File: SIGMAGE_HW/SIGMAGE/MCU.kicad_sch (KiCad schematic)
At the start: 28 parts, among them J10 TSW10607GS, J11 HTSW10807GD, J12 HTSW10807GD, J13 HTSW10807GD, J9 TSW10607GS, U8 STM32F407VGTx, X1 STDCSU18M

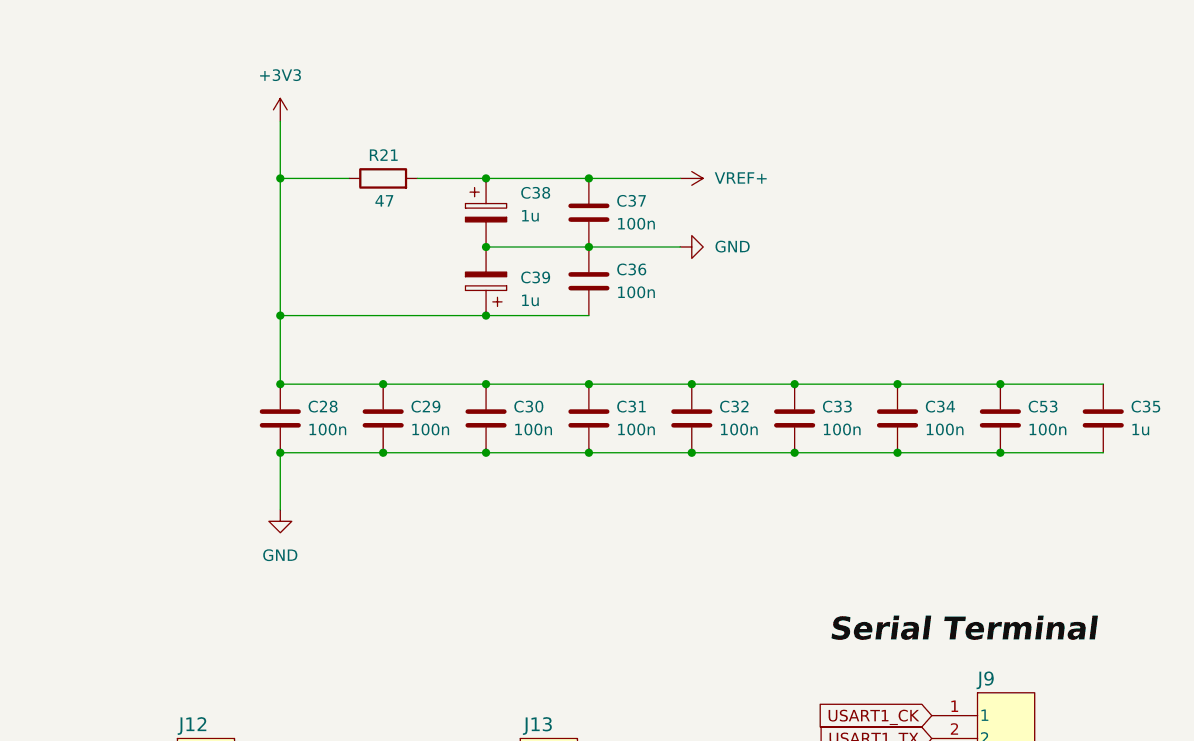
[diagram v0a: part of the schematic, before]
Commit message: More DAC changes
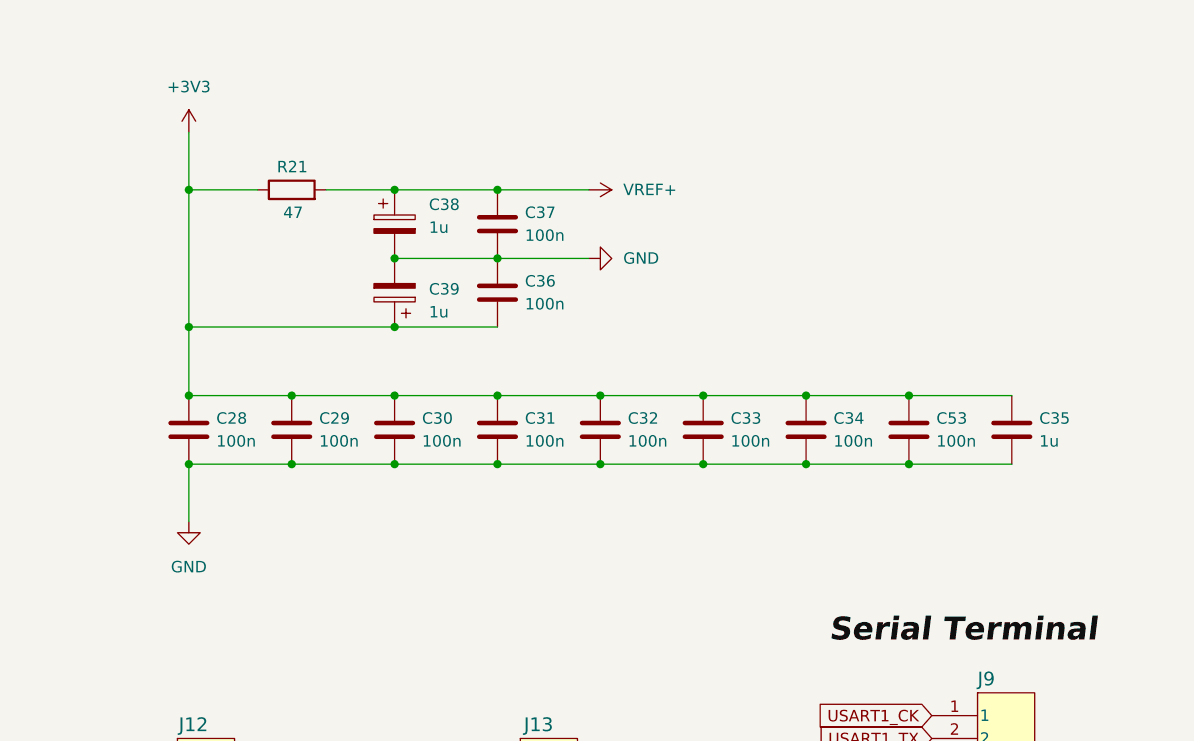
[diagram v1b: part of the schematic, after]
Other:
- moved on the sheet: C28, C29, C30, C31, C32, C33, C34, C35, C36, C37, C38, C39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

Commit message: preps for FPGA
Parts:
- removed J11, J12, J13: HTSW10807GD, SIGMAGE:HTSW10807GD, symbol SIGMAGE:HTSW10807GD
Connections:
- net GPIO_PE0 is gone; now on net ADC1_LRCK: U8.97 (PE0)
- net GPIO_PE1 is gone; now on net ADC2_LRCK: U8.98 (PE1)
- net GPIO_PE2 is gone; now on net ADC1_BYPAS: U8.1 (PE2)
- net GPIO_PE3 is gone; now on net ADC2_BYPAS: U8.2 (PE3)
- net ADC1_BCK: no longer U8.52 (PB13)
- net ADC1_BYPAS: no longer U8.93 (PB7)
- net ADC1_DOUT: no longer U8.54 (PB15)
- net ADC1_LRCK: no longer U8.51 (PB12)
- net ADC1_PDWN: no longer U8.92 (PB6)
- net ADC2_BCK: no longer U8.78 (PC10)
- net ADC2_BYPAS: no longer U8.96 (PB9)
- net ADC2_DOUT: no longer U8.91 (PB5)
- net ADC2_LRCK: no longer U8.29 (PA4)
- net ADC2_PDWN: no longer U8.95 (PB8)
- net ADC2_SCKI: no longer U8.64 (PC7)
- net JTCK_SWCLK: no longer U8.76 (PA14)
- net JTDI: no longer U8.77 (PA15)
- net JTDO_SWO: no longer U8.89 (PB3)
- net JTMS_SWDIO: no longer U8.72 (PA13)
- net JTRST: no longer U8.90 (PB4)
- net PHY_CRS_DV: no longer U8.32 (PA7)
- net PHY_MDC: no longer U8.16 (PC1)
- net PHY_MDIO: no longer U8.25 (PA2)
- net PHY_NRST: no longer U8.47 (PB10)
- net PHY_REFCLK: no longer U8.24 (PA1)
- net PHY_RXD0: no longer U8.33 (PC4)
- net PHY_RXD1: no longer U8.34 (PC5)
- net PHY_TXD0: no longer U8.80 (PC12)
- net PHY_TXD1: no longer U8.7 (PC13)
- net PHY_TXEN: no longer U8.48 (PB11)
- net USART1_CK: no longer U8.67 (PA8)
- net USART1_CTS: no longer U8.70 (PA11)
- net USART1_RTS: no longer U8.71 (PA12)
- net USART1_RX: no longer U8.69 (PA10)
- net USART1_TX: no longer U8.68 (PA9)
- net ADC1_SCKI: no longer names the net of U8.63 (PC6)
- net GPIO_PA0: no longer names the net of U8.23 (PA0)
- net GPIO_PA3: no longer names the net of U8.26 (PA3)
- net GPIO_PA5: no longer names the net of U8.30 (PA5)
- net GPIO_PA6: no longer names the net of U8.31 (PA6)
- net GPIO_PB0: no longer names the net of U8.35 (PB0)
- net GPIO_PB1: no longer names the net of U8.36 (PB1)
- net GPIO_PB14: no longer names the net of U8.53 (PB14)
- net GPIO_PB2: no longer names the net of U8.37 (PB2)
- net GPIO_PC0: no longer names the net of U8.15 (PC0)
- net GPIO_PC11: no longer names the net of U8.79 (PC11)
- net GPIO_PC14: no longer names the net of U8.8 (PC14)
- net GPIO_PC15: no longer names the net of U8.9 (PC15)
- net GPIO_PC2: no longer names the net of U8.17 (PC2)
- net GPIO_PC3: no longer names the net of U8.18 (PC3)
- net GPIO_PC8: no longer names the net of U8.65 (PC8)
- net GPIO_PC9: no longer names the net of U8.66 (PC9)
- net GPIO_PD0: no longer names the net of U8.81 (PD0)
- net GPIO_PD1: no longer names the net of U8.82 (PD1)
- net GPIO_PD10: no longer names the net of U8.57 (PD10)
- net GPIO_PD11: no longer names the net of U8.58 (PD11)
- net GPIO_PD12: no longer names the net of U8.59 (PD12)
- net GPIO_PD13: no longer names the net of U8.60 (PD13)
- net GPIO_PD14: no longer names the net of U8.61 (PD14)
- net GPIO_PD15: no longer names the net of U8.62 (PD15)
- net GPIO_PD2: no longer names the net of U8.83 (PD2)
- net GPIO_PD3: no longer names the net of U8.84 (PD3)
- net GPIO_PD4: no longer names the net of U8.85 (PD4)
- net GPIO_PD5: no longer names the net of U8.86 (PD5)
- net GPIO_PD6: no longer names the net of U8.87 (PD6)
- net GPIO_PD7: no longer names the net of U8.88 (PD7)
- net GPIO_PD8: no longer names the net of U8.55 (PD8)
- net GPIO_PD9: no longer names the net of U8.56 (PD9)
- net GPIO_PE10: no longer names the net of U8.41 (PE10)
- net GPIO_PE11: no longer names the net of U8.42 (PE11)
- net GPIO_PE12: no longer names the net of U8.43 (PE12)
- net GPIO_PE13: no longer names the net of U8.44 (PE13)
- net GPIO_PE14: no longer names the net of U8.45 (PE14)
- net GPIO_PE15: no longer names the net of U8.46 (PE15)
- net GPIO_PE4: no longer names the net of U8.3 (PE4)
- net GPIO_PE5: no longer names the net of U8.4 (PE5)
- net GPIO_PE6: no longer names the net of U8.5 (PE6)
- net GPIO_PE7: no longer names the net of U8.38 (PE7)
- net GPIO_PE8: no longer names the net of U8.39 (PE8)
- net GPIO_PE9: no longer names the net of U8.40 (PE9)

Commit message: some changes
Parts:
- removed C28, C29, C30, C31, C32, C33, C34, C36, C37, C40, C53: 100n, Capacitor_SMD:C_0603_1608Metric, symbol Device:C
- removed C35: 1u, Capacitor_SMD:C_0603_1608Metric, symbol Device:C
- removed C38, C39: 1u, Capacitor_SMD:C_0603_1608Metric, symbol Device:C_Polarized
- removed C41, C42: 20p, Capacitor_SMD:C_0603_1608Metric, symbol Device:C
- removed C43, C44: 2p2, Capacitor_SMD:C_0603_1608Metric, symbol Device:C
- removed J10, J9: TSW10607GS, SIGMAGE:TSW10607GS, symbol SIGMAGE:TSW10607GS
- removed R21: 47, Resistor_SMD:R_0603_1608Metric, symbol Device:R
- removed R22, R23: 10k, Resistor_SMD:R_0603_1608Metric, symbol Device:R
- removed U8: STM32F407VGTx, Package_QFP:LQFP-100_14x14mm_P0.5mm, symbol MCU_ST_STM32F4:STM32F407VGTx
- removed X1: STDCSU18M, SIGMAGE:STDCSU18M, symbol SIGMAGE:STDCSU18M

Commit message: changes
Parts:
- added C112, C113: 18p, Capacitor_SMD:C_0603_1608Metric, symbol Device:C
- added C114, C115: 2.2p, Capacitor_SMD:C_0603_1608Metric, symbol Device:C
- added C116, C117, C118, C119, C120, C121, C122, C123, C125, C126: 100n, Capacitor_SMD:C_0603_1608Metric, symbol Device:C
- added C124: 10u, Capacitor_SMD:C_0603_1608Metric, symbol Device:C
- added C88: 100n, Capacitor_SMD:C_1206_3216Metric, symbol Device:C
- added C89, C90: 1u, symbol Device:C_Polarized
- added J5: TSW10607GS, SIGMAGE:TSW10607GS, symbol SIGMAGE:TSW10607GS
- added R56, R57: 10k, Resistor_SMD:R_0603_1608Metric, symbol Device:R
- added R58: 47, Resistor_SMD:R_0603_1608Metric, symbol Device:R
- added U15: STM32F407VGTx, Package_QFP:LQFP-100_14x14mm_P0.5mm, symbol MCU_ST_STM32F4:STM32F407VGTx
- added X1: STDCSU18M, SIGMAGE:STDCSU18M, symbol SIGMAGE:STDCSU18M
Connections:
- new net: C112.1, U15.12 (PH0), X1.1
- new net: C113.1, U15.13 (PH1), X1.2
- new net: C88.2, R56.2, U15.14 (NRST)
- new net: C114.1, U15.49 (VCAP_1)
- new net: C115.1, U15.73 (VCAP_2)
- new net: R57.2, U15.94 (BOOT0)
- new net DVCC_3V3: C116.1, C117.1, C118.1, C119.1, C120.1, C121.1, C122.1, C123.1, C124.1, C126.2, C90.1, R56.1, R58.1, U15.100 (VDD), U15.11 (VDD), U15.19 (VDD), U15.22 (VDDA), U15.28 (VDD), U15.50 (VDD), U15.6 (VBAT), U15.75 (VDD)
- new net DVREF_3V3: C125.1, C89.1, R58.2, U15.21 (VREF+)
- new net GND: C112.2, C113.2, C114.2, C115.2, C116.2, C117.2, C118.2, C119.2, C120.2, C121.2, C122.2, C123.2, C124.2, C125.2, C126.1, C88.1, C89.2, C90.2, J5.6, R57.1, U15.10 (VSS), U15.20 (VSSA), U15.27 (VSS), U15.74 (VSS), U15.99 (VSS)
- new net MCU_JTAG_TCK: U15.76 (PA14)
- new net MCU_JTAG_TDI: U15.77 (PA15)
- new net MCU_JTAG_TDO: U15.89 (PB3)
- new net MCU_JTAG_TMS: U15.72 (PA13)
- new net MCU_USART1_RX: J5.2, U15.69 (PA10)
- new net MCU_USART1_TX: J5.1, U15.68 (PA9)
- no-connect marks 0 -> 3

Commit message: major changes
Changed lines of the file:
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@@
+		)
+	)
+	(label "FPGA_INITN"
+		(at 182.88 118.11 180)
+		(effects
+			(font
+				(size 1.27 1.27)
+			)
+			(justify right bottom)
 		)
 	)
@@
 			)
 			(justify left bottom)
+		)
+	)
+	(label "FPGA_CFG0"
+		(at 182.88 102.87 180)
+		(effects
+			(font
+				(size 1.27 1.27)
+			)
+			(justify right bottom)
 		)
 	)
@@
 	(label "MCU_JTAG_TDO"
 		(at 144.78 93.98 180)
+		(effects
+			(font
+				(size 1.27 1.27)
+			)
+			(justify right bottom)
+		)
+	)
+	(label "FPGA_CFG1"
+		(at 182.88 107.95 180)
 		(effects
 			(font
@@
 		)
 	)
+	(label "FPGA_CFG2"
+		(at 182.88 105.41 180)
+		(effects
+			(font
+				(size 1.27 1.27)
+			)
+			(justify right bottom)
+		)
+	)
+	(label "FPGA_DONE"
+		(at 182.88 110.49 180)
+		(effects
+			(font
+				(size 1.27 1.27)
+			)
+			(justify right bottom)
+		)
+	)
+	(label "FPGA_PROGRAMN"
+		(at 182.88 113.03 180)
+		(effects
+			(font
+				(size 1.27 1.27)
+			)
+			(justify right bottom)
+		)
+	)

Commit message: changes
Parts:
- removed C125, C126: 100n, Capacitor_SMD:C_0603_1608Metric, symbol Device:C
- removed C89, C90: 1u, symbol Device:C_Polarized
- removed R58: 47, Resistor_SMD:R_0603_1608Metric, symbol Device:R
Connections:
- net DVREF_3V3 is gone; now on net DVCC_3V3: U15.21 (VREF+)
- net SDCARD_SPI_CS: now reaches U15.29 (PA4)
- net SDCARD_SPI_SCK: now reaches U15.30 (PA5)
- net SDCARD_SPI_MISO: now reaches U15.31 (PA6)
- net SDCARD_SPI_MOSI: now reaches U15.32 (PA7)
- net FPGA_SPI_CS: now reaches U15.51 (PB12)
- net FPGA_SPI_CLK: now reaches U15.52 (PB13)
- net FPGA_SPI_MISO: now reaches U15.53 (PB14)
- net FPGA_SPI_MOSI: now reaches U15.54 (PB15)
- net ICOM_AUX8: now reaches U15.55 (PD8)
- net ICOM_AUX9: now reaches U15.56 (PD9)
- net ICOM_AUX10: now reaches U15.57 (PD10)
- net ICOM_AUX11: now reaches U15.58 (PD11)
- net ICOM_AUX12: now reaches U15.59 (PD12)
- net ICOM_AUX13: now reaches U15.60 (PD13)
- net ICOM_AUX14: now reaches U15.61 (PD14)
- net ICOM_AUX15: now reaches U15.62 (PD15)
- net ICOM_AUX0: now reaches U15.81 (PD0)
- net ICOM_AUX1: now reaches U15.82 (PD1)
- net ICOM_AUX2: now reaches U15.83 (PD2)
- net ICOM_AUX3: now reaches U15.84 (PD3)
- net ICOM_AUX4: now reaches U15.85 (PD4)
- net ICOM_AUX5: now reaches U15.86 (PD5)
- net ICOM_AUX6: now reaches U15.87 (PD6)
- net ICOM_AUX7: now reaches U15.88 (PD7)
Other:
- moved on the sheet: C116, C117, C118, C119, C120, C121, C122, C123, C124

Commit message: almost done
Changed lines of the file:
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@@
+		)
+	)
+	(label "FPGA_HOLDN"
+		(at 187.96 120.65 180)
+		(effects
+			(font
+				(size 1.27 1.27)
+			)
+			(justify right bottom)
 		)
 	)

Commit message: changes
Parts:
- added D263, D264, D265, D266, D267, D268, D269, D270, D271, D272, D273, D274, D275, D276, D277, D278: LED, LED_SMD:LED_0603_1608Metric, symbol Device:LED
- added R169, R170, R171, R172, R173, R174, R175, R176, R177, R178, R179, R180, R181, R182, R183, R184: 650, Resistor_SMD:R_0603_1608Metric, symbol Device:R
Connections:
- net DVCC_3V3: now also J5.1
- net GND: now also R169.1, R170.1, R171.1, R172.1, R173.1, R174.1, R175.1, R176.1, R177.1, R178.1, R179.1, R180.1, R181.1, R182.1, R183.1, R184.1
- net ICOM_AUX0: now also U15.97 (PE0); no longer U15.81 (PD0)
- net ICOM_AUX1: now also U15.98 (PE1); no longer U15.82 (PD1)
- net ICOM_AUX10: now also U15.41 (PE10); no longer U15.57 (PD10)
- net ICOM_AUX11: now also U15.42 (PE11); no longer U15.58 (PD11)
- net ICOM_AUX12: now also U15.43 (PE12); no longer U15.59 (PD12)
- net ICOM_AUX13: now also U15.44 (PE13); no longer U15.60 (PD13)
- net ICOM_AUX14: now also U15.45 (PE14); no longer U15.61 (PD14)
- net ICOM_AUX15: now also U15.46 (PE15); no longer U15.62 (PD15)
- net ICOM_AUX2: now also U15.1 (PE2); no longer U15.83 (PD2)
- net ICOM_AUX3: now also U15.2 (PE3); no longer U15.84 (PD3)
- net ICOM_AUX4: now also U15.3 (PE4); no longer U15.85 (PD4)
- net ICOM_AUX5: now also U15.4 (PE5); no longer U15.86 (PD5)
- net ICOM_AUX6: now also U15.5 (PE6); no longer U15.87 (PD6)
- net ICOM_AUX7: now also U15.38 (PE7); no longer U15.88 (PD7)
- net ICOM_AUX8: now also U15.39 (PE8); no longer U15.55 (PD8)
- net ICOM_AUX9: now also U15.40 (PE9); no longer U15.56 (PD9)
- net MCU_USART1_RX: now also J5.3; no longer J5.2
- net MCU_USART1_TX: now also J5.2; no longer J5.1
- net ICOM_USART3_TX: now reaches U15.78 (PC10)
- net ICOM_USART3_RX: now reaches U15.79 (PC11)
- new net: D263.1 (K), R169.2
- new net: D263.2 (A), U15.81 (PD0)
- new net: D274.1 (K), R180.2
- new net: D272.1 (K), R178.2
- new net: D268.1 (K), R174.2
- new net: D273.1 (K), R179.2
- new net: D273.2 (A), U15.57 (PD10)
- new net: D275.1 (K), R181.2
- new net: D275.2 (A), U15.59 (PD12)
- new net: D277.1 (K), R183.2
- new net: D265.1 (K), R171.2
- new net: D265.2 (A), U15.83 (PD2)
- new net: D266.1 (K), R172.2
- new net: D266.2 (A), U15.84 (PD3)
- new net: D269.1 (K), R175.2
- new net: D278.1 (K), R184.2
- new net: D271.2 (A), U15.55 (PD8)
- new net: D272.2 (A), U15.56 (PD9)
- new net: D274.2 (A), U15.58 (PD11)
- new net: D276.2 (A), U15.60 (PD13)
- new net: D277.2 (A), U15.61 (PD14)
- new net: D278.2 (A), U15.62 (PD15)
- new net: D264.2 (A), U15.82 (PD1)
- new net: D267.2 (A), U15.85 (PD4)
- new net: D268.2 (A), U15.86 (PD5)
- new net: D269.2 (A), U15.87 (PD6)
- new net: D270.2 (A), U15.88 (PD7)
- new net: D267.1 (K), R173.2
- new net: D271.1 (K), R177.2
- new net: D276.1 (K), R182.2
- new net: D270.1 (K), R176.2
- new net: D264.1 (K), R170.2
- no-connect marks 3 -> 2
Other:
- moved on the sheet: C112, C113, C114, C115, C88, R56, R57, U15, X1
